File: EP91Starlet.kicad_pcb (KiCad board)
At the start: 2 copper layers, 116.8 x 96.5 mm, 4 parts, among them M1 Module-mega-mcu64-0.1, M2 Module-wbo-0.5, M3 Module-vr-max9924-0.1, M4 Module-knock-0.2

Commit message: more testing
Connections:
- M1 pad G: unconnected-(M1-GND-PadG) -> GND
- M1 pad N22: unconnected-(M1-V33-PadN22) -> Net-(M4-VREF)
- M1 pad S26: unconnected-(M1-IN_ADC10/EINT0_(VR_CRK)-PadS26) -> Net-(M1-IN_ADC10/EINT0_(VR_CRK))
- M1 pad W12: unconnected-(M1-CAN1H-PadW12) -> Net-(M1-CAN1H)
- M1 pad W13: unconnected-(M1-CAN1L-PadW13) -> Net-(M1-CAN1L)
- M2 pad G: unconnected-(M2-GND-PadG) -> GND
- M2 pad W3: unconnected-(M2-CANL-PadW3) -> Net-(M1-CAN1H)
- M2 pad W4: unconnected-(M2-CANH-PadW4) -> Net-(M1-CAN1L)
- M3 pad E3: unconnected-(M3-OUT-PadE3) -> Net-(M1-IN_ADC10/EINT0_(VR_CRK))
- M3 pad G: unconnected-(M3-GND-PadG) -> GND
- M4 pad E2: unconnected-(M4-GND-PadE2) -> GND
- M4 pad W2: unconnected-(M4-VREF-PadW2) -> Net-(M4-VREF)

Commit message: Fix pcb layers
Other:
- copper layers 2 -> 4

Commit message: 65urft7ih
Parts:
- added U1: ~, EP91Starlet:4EFE ECU Connector, F.Cu at (90.4, 86.9)
- moved M3 18.6 mm to (109.5, 65.2)
- moved M4 17.6 mm to (105.3, 71.3)
- moved M2 16.9 mm to (106.9, 87.5)
- moved M1 11.2 mm to (128.9, 111.5)
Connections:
- M1 pad G: GND -> unconnected-(M1-GND-PadG)
- M1 pad W12: Net-(M1-CAN1H) -> /CAN+
- M1 pad W13: Net-(M1-CAN1L) -> /CAN-
- M2 pad G: GND -> unconnected-(M2-GND-PadG)
- M2 pad W3: Net-(M1-CAN1H) -> /CAN-
- M2 pad W4: Net-(M1-CAN1L) -> /CAN+
- M3 pad G: GND -> unconnected-(M3-GND-PadG)
- M4 pad E2: GND -> unconnected-(M4-GND-PadE2)
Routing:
- net /CAN-: track 0.00 -> 17.3 mm
- net /CAN+: track 0.00 -> 16.3 mm
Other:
- board size 116.8 x 96.5 mm -> 208.8 x 96.5 mm

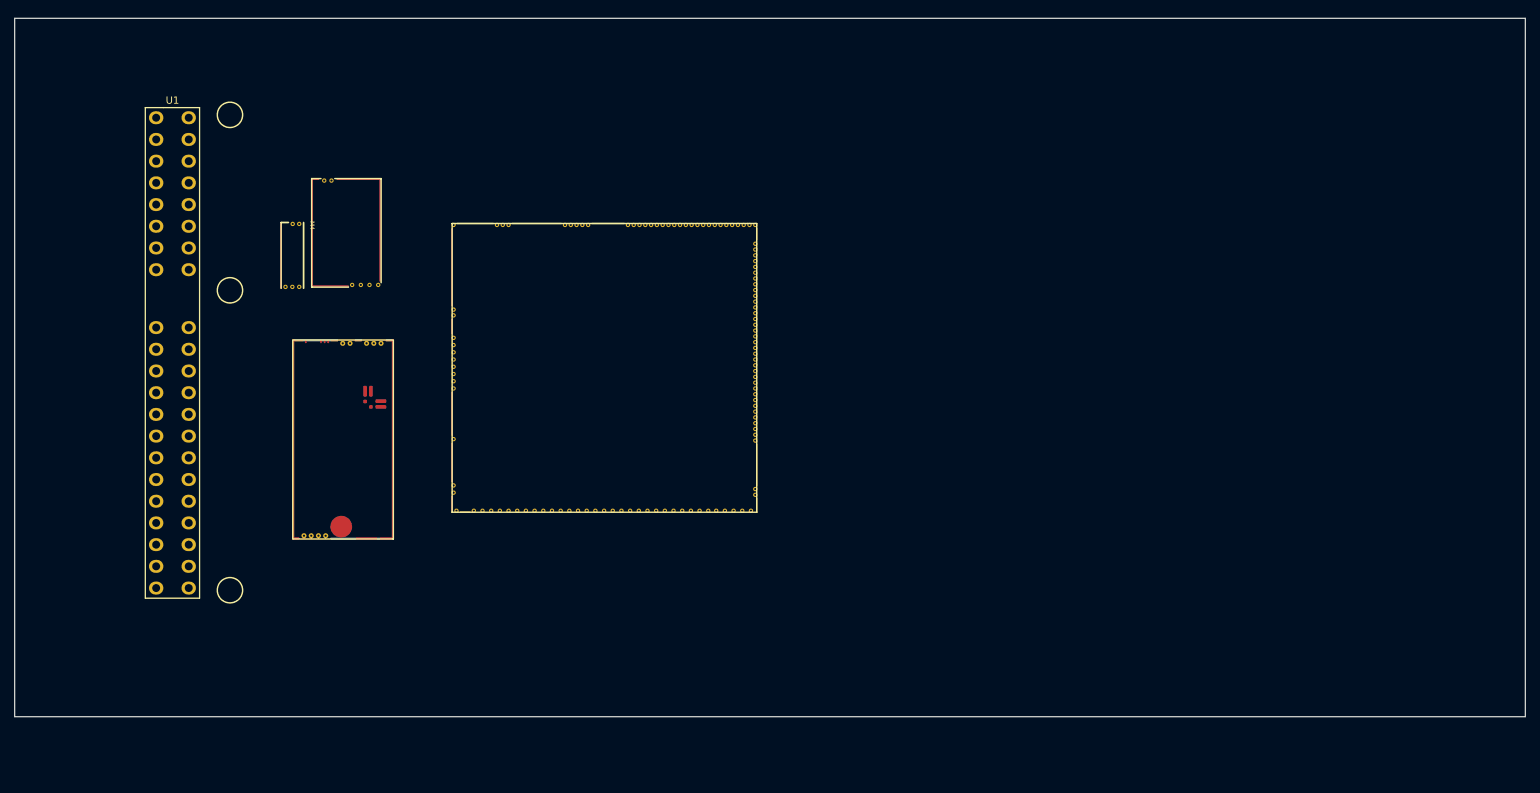
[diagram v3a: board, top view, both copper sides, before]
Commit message: Pin mapping
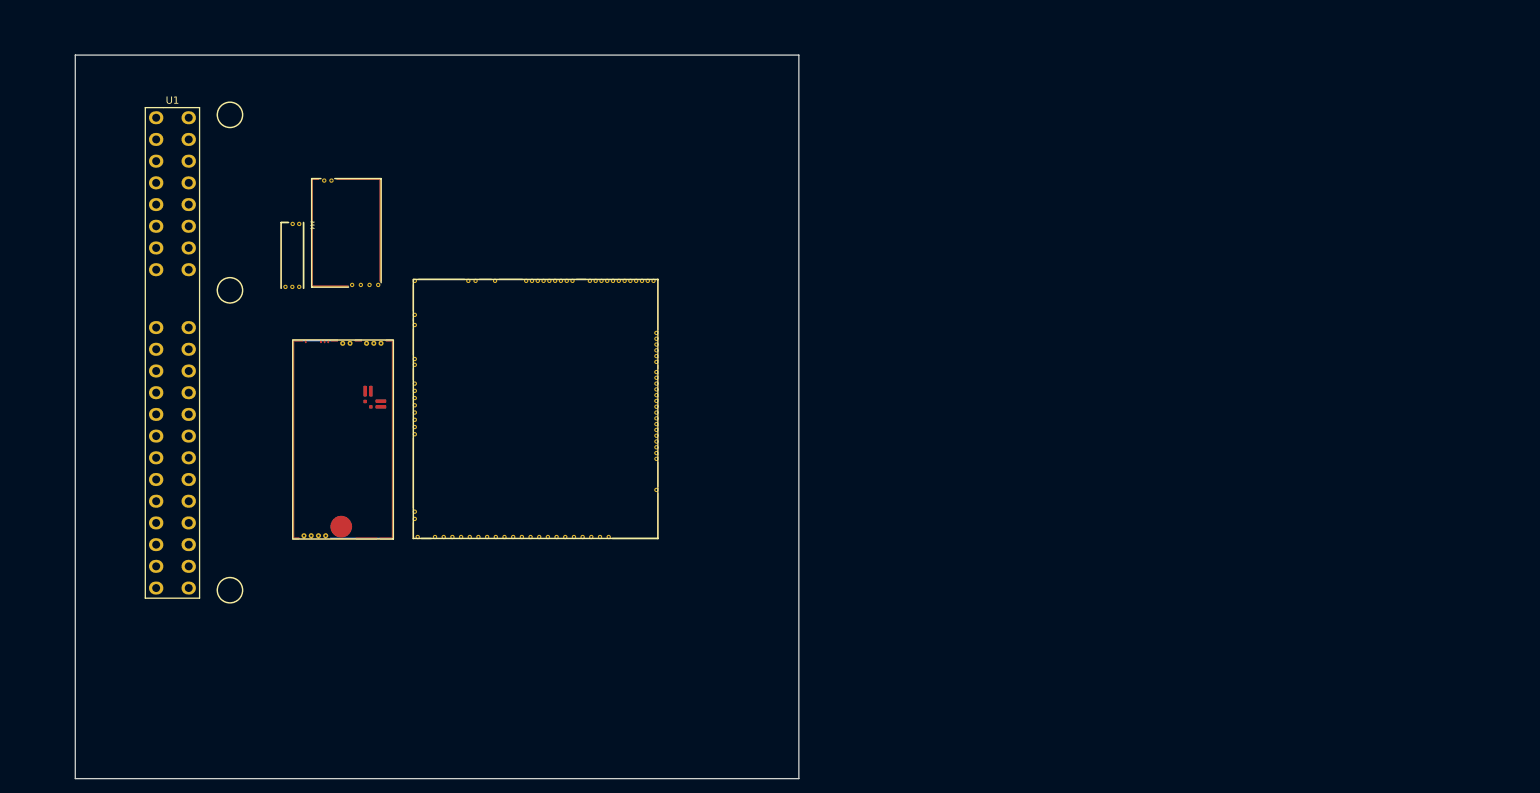
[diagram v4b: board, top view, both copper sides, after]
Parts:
- M1: value Module-mega-mcu64-0.1 -> Module:mega-mcu100/0.3; footprint 0.1:mega-mcu64 -> 0.33:mega-mcu100
- moved M1 6.47 mm to (123.6, 115.2)
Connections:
- M1 pad E10: (no net) -> unconnected-(M1-OUT_INJ8_(PD12)-PadE10)
- M1 pad E11: (no net) -> unconnected-(M1-OUT_INJ7_(PD15)-PadE11)
- M1 pad E12: (no net) -> unconnected-(M1-OUT_INJ6_(PA8)-PadE12)
- M1 pad E13: (no net) -> unconnected-(M1-OUT_INJ5_(PD2)-PadE13)
- M1 pad E18: (no net) -> unconnected-(M1-OUT_PWM1_(PD13)-PadE18)
- M1 pad E19: (no net) -> unconnected-(M1-OUT_PWM2_(PC6)-PadE19)
- M1 pad E20: (no net) -> unconnected-(M1-OUT_PWM3_(PC7)-PadE20)
- M1 pad E21: (no net) -> unconnected-(M1-OUT_PWM4_(PC8)-PadE21)
- M1 pad E22: (no net) -> unconnected-(M1-OUT_PWM5_(PC9)-PadE22)
- M1 pad E23: (no net) -> unconnected-(M1-OUT_PWM6_(PD14)-PadE23)
- M1 pad E6: (no net) -> unconnected-(M1-SPI2_CS_/_CAN2_RX_(PB12)-PadE6)
- M1 pad E7: (no net) -> unconnected-(M1-SPI2_SCK_/_CAN2_TX_(PB13)-PadE7)
- M1 pad E8: (no net) -> unconnected-(M1-SPI2_MISO_(PB14)-PadE8)
- M1 pad E9: (no net) -> unconnected-(M1-SPI2_MOSI_(PB15)-PadE9)
- M1 pad N20: (no net) -> unconnected-(M1-OUT_PWR_EN_(PE10)-PadN20)
- M1 pad N21: (no net) -> unconnected-(M1-V33-PadN21)
- M1 pad N22: Net-(M4-VREF) -> unconnected-(M1-VCC-PadN22)
- M1 pad N23: (no net) -> unconnected-(M1-V33-PadN23)
- M1 pad S1: (no net) -> unconnected-(M1-IN_D4_(PE15)-PadS1)
- M1 pad S10: (no net) -> unconnected-(M1-IN_O2S2_(PA1)-PadS10)
- M1 pad S11: (no net) -> unconnected-(M1-IN_O2S_/_CAN_WAKEUP_(PA0)-PadS11)
- M1 pad S12: (no net) -> unconnected-(M1-IN_MAP2_(PC1)-PadS12)
- M1 pad S13: (no net) -> unconnected-(M1-IN_MAP1_(PC0)-PadS13)
- M1 pad S14: (no net) -> unconnected-(M1-IN_CRANK_(PB1)-PadS14)
- M1 pad S15: (no net) -> unconnected-(M1-IN_KNOCK_(PA2)-PadS15)
- M1 pad S16: (no net) -> unconnected-(M1-IN_CAM_(PA6)-PadS16)
- M1 pad S17: (no net) -> unconnected-(M1-IN_VSS_(PE11)-PadS17)
- M1 pad S18: (no net) -> unconnected-(M1-IN_TPS_(PA4)-PadS18)
- M1 pad S19: (no net) -> unconnected-(M1-IN_PPS_(PA3)-PadS19)
- M1 pad S2: (no net) -> unconnected-(M1-IN_D3_(PE14)-PadS2)
- M1 pad S20: (no net) -> unconnected-(M1-IN_IAT_(PC3)-PadS20)
- M1 pad S21: (no net) -> unconnected-(M1-IN_CLT_(PC2)-PadS21)
- M1 pad S3: (no net) -> unconnected-(M1-IN_D2_(PE13)-PadS3)
- M1 pad S4: (no net) -> unconnected-(M1-IN_D1_(PE12)-PadS4)
- M1 pad S6: (no net) -> unconnected-(M1-IN_AUX4_(PC5)-PadS6)
- M1 pad S7: (no net) -> unconnected-(M1-IN_AUX3_(PA7)-PadS7)
- M1 pad S8: (no net) -> unconnected-(M1-IN_AUX2_(PC4/PE9)-PadS8)
- M1 pad S9: (no net) -> unconnected-(M1-IN_AUX1_(PB0)-PadS9)
- M1 pad W10: (no net) -> unconnected-(M1-IGN1_(PC13)-PadW10)
- M1 pad W11: (no net) -> unconnected-(M1-CANH-PadW11)
- M1 pad W12: /CAN+ -> unconnected-(M1-CANL-PadW12)
- M1 pad W13: /CAN- -> unconnected-(M1-V33_REF-PadW13)
- M1 pad W3: (no net) -> unconnected-(M1-IGN8_(PE6)-PadW3)
- M1 pad W4: (no net) -> unconnected-(M1-IGN7_(PB9)-PadW4)
- M1 pad W5: (no net) -> unconnected-(M1-IGN6_(PB8)-PadW5)
- M1 pad W6: (no net) -> unconnected-(M1-IGN5_(PE2)-PadW6)
- M1 pad W7: (no net) -> unconnected-(M1-IGN4_(PE3)-PadW7)
- M2 pad W3: /CAN- -> unconnected-(M2-CANL-PadW3)
- M2 pad W4: /CAN+ -> unconnected-(M2-CANH-PadW4)
- M3 pad E3: Net-(M1-IN_ADC10/EINT0_(VR_CRK)) -> unconnected-(M3-OUT-PadE3)
- M4 pad W2: Net-(M4-VREF) -> unconnected-(M4-VREF-PadW2)
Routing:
- net /CAN-: track 17.3 -> 0.00 mm
- net /CAN+: track 16.3 -> 0.00 mm
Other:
- board size 208.8 x 96.5 mm -> 100 x 100 mm

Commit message: add submodules for ign and inj + flyback protected output
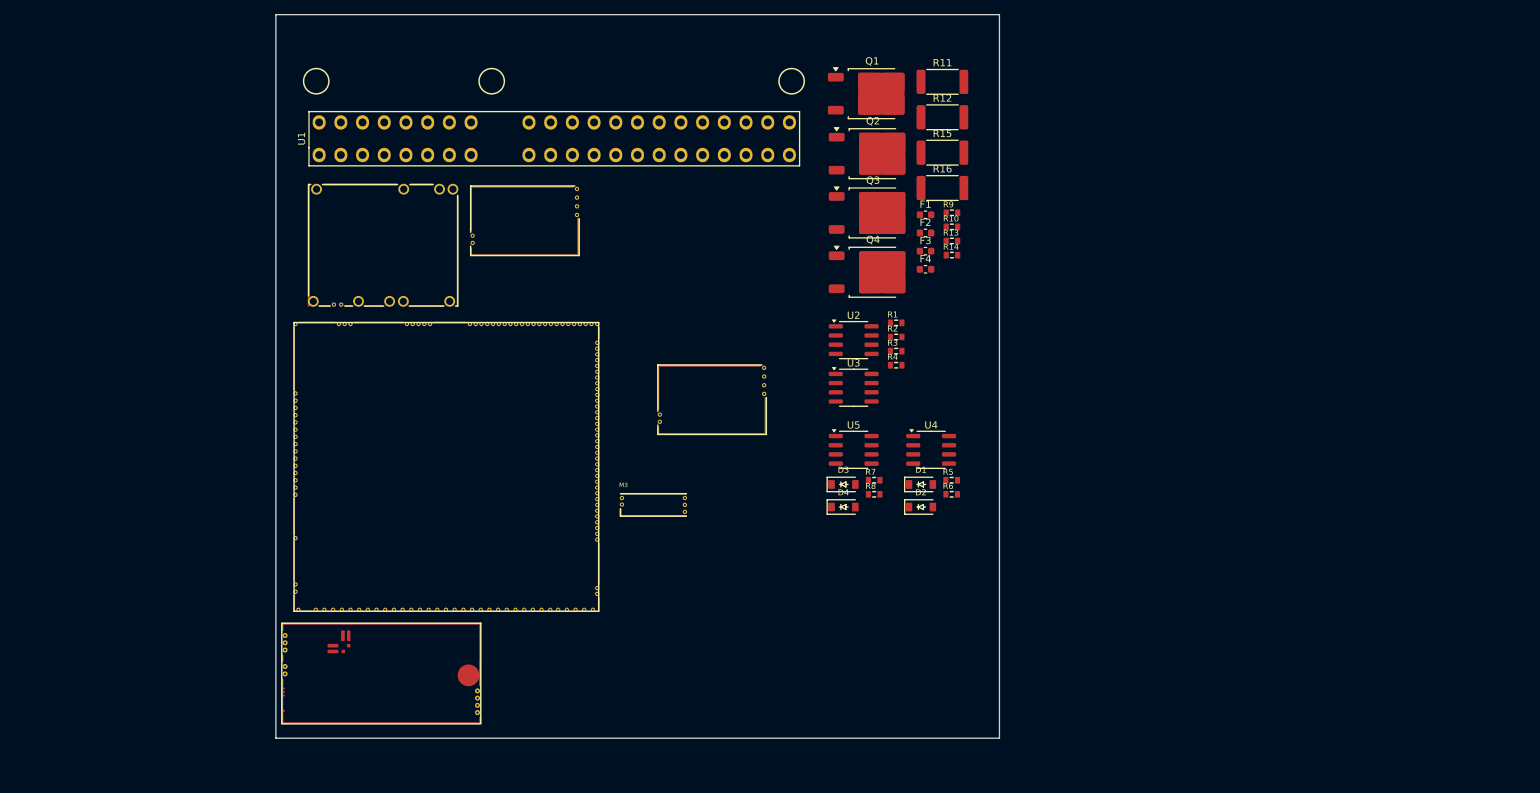
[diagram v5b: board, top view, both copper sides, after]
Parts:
- added D1: B5819W, footprints:SOD-123, F.Cu at (193.8, 107.6)
- added D2: B5819W, footprints:SOD-123, F.Cu at (193.8, 110.7)
- added D3: B5819W, footprints:SOD-123, F.Cu at (183.1, 107.6)
- added D4: B5819W, footprints:SOD-123, F.Cu at (183.1, 110.7)
- added F1: 50mA, Fuse:Fuse_0603_1608Metric, F.Cu at (194.5, 70.3)
- added F2: 50mA, Fuse:Fuse_0603_1608Metric, F.Cu at (194.5, 72.8)
- added F3: 50mA, Fuse:Fuse_0603_1608Metric, F.Cu at (194.5, 75.4)
- added F4: 50mA, Fuse:Fuse_0603_1608Metric, F.Cu at (194.5, 77.9)
- added M5: Module-vr-max9924-0.1, vr_max:vr-max9924, F.Cu at (131.5, 76.1)
- added M6: Module-power_12and5V-0.3, power12_5:power_12and5V, F.Cu at (109.1, 66.0)
- added Q1: ISL9V3040D3ST, Package_TO_SOT_SMD:TO-252-2, F.Cu at (187.1, 53.6)
- added Q2: ISL9V3040D3ST, Package_TO_SOT_SMD:TO-252-2, F.Cu at (187.2, 61.9)
- added Q3: ISL9V3040D3ST, Package_TO_SOT_SMD:TO-252-2, F.Cu at (187.2, 70.1)
- added Q4: ISL9V3040D3ST, Package_TO_SOT_SMD:TO-252-2, F.Cu at (187.2, 78.3)
- added R1: 4.7k, footprints:R0603, F.Cu at (190.4, 85.3)
- added R10: 22, footprints:R0603, F.Cu at (198.1, 72.0)
- added R11: 0, Resistor_SMD:R_2512_6332Metric, F.Cu at (196.8, 52.0)
- added R12: 0, Resistor_SMD:R_2512_6332Metric, F.Cu at (196.8, 56.9)
- added R13: 22, footprints:R0603, F.Cu at (198.1, 74.0)
- added R14: 22, footprints:R0603, F.Cu at (198.1, 75.9)
- added R15: 0, Resistor_SMD:R_2512_6332Metric, F.Cu at (196.8, 61.7)
- added R16: 0, Resistor_SMD:R_2512_6332Metric, F.Cu at (196.8, 66.6)
- added R2: 4.7k, footprints:R0603, F.Cu at (190.4, 87.2)
- added R3: 4.7k, footprints:R0603, F.Cu at (190.4, 89.2)
- added R4: 4.7k, footprints:R0603, F.Cu at (190.4, 91.1)
- added R5: 4.7k, footprints:R0603, F.Cu at (198.1, 107.0)
- added R6: 4.7k, footprints:R0603, F.Cu at (198.1, 109.0)
- added R7: 4.7k, footprints:R0603, F.Cu at (187.4, 107.0)
- added R8: 4.7k, footprints:R0603, F.Cu at (187.4, 109.0)
- added R9: 22, footprints:R0603, F.Cu at (198.1, 70.1)
- added U2: VNLD5160TR-E, Package_SO:SOIC-8_3.9x4.9mm_P1.27mm, F.Cu at (184.5, 87.7)
- added U3: VNLD5160TR-E, Package_SO:SOIC-8_3.9x4.9mm_P1.27mm, F.Cu at (184.5, 94.2)
- added U4: VNLD5160TR-E, Package_SO:SOIC-8_3.9x4.9mm_P1.27mm, F.Cu at (195.2, 102.8)
- added U5: VNLD5160TR-E, Package_SO:SOIC-8_3.9x4.9mm_P1.27mm, F.Cu at (184.5, 102.8)
- M1: value Module:mega-mcu100/0.3 -> Module-vr-max9924-0.1; footprint 0.33:mega-mcu100 -> vr_max:vr-max9924
- M2: value Module-wbo-0.5 -> Module-mega-mcu144-0.7; footprint 0.5:wbo -> mega144:mega-mcu144
- M3: value Module-vr-max9924-0.1 -> Module-knock-0.2; footprint 0.3:vr-max9924 -> knock:knock
- M4: value Module-knock-0.2 -> Module-wbo-0.5; footprint 0.2:knock -> wbo:wbo
- U1: footprint EP91Starlet:4EFE ECU Connector -> EP91 libraries:4EFE ECU Connector
- moved M4 69.5 mm to (105.4, 140.8), turned to 0 degrees
- moved M3 63.4 mm to (152.2, 112.1), turned to 0 degrees
- moved U1 57.1 mm to (140.7, 59.8), turned to 0 degrees
- moved M2 37.7 mm to (107.1, 125.2), turned to 0 degrees
- moved M1 36.7 mm to (157.4, 100.8)
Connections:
- M1 pad E3: unconnected-(M1-I2C_SCL_(PB10)-PadE3) -> Net-(M1-OUT)
- M1 pad E4: unconnected-(M1-I2C_SDA_(PB11)-PadE4) -> +5VP
- M1 pad G: unconnected-(M1-GND-PadG) -> GND
- M2 pad G: unconnected-(M2-GND-PadG) -> GND
- M2 pad W8: unconnected-(M2-V33_OUT-PadW8) -> /IGN4/IN4
- M2 pad W9: unconnected-(M2-VDDA-PadW9) -> /IGN4/IN3
- U1 pad 2: unconnected-(U1-#20-Pad2) -> /INJ4/OUT1
- U1 pad 23: unconnected-(U1-BATT-Pad23) -> Net-(M6-IN_VIGN)
- U1 pad 41: unconnected-(U1-#10-Pad41) -> /INJ4/OUT2
